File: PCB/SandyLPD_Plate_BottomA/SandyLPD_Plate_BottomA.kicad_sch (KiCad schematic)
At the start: 14 parts

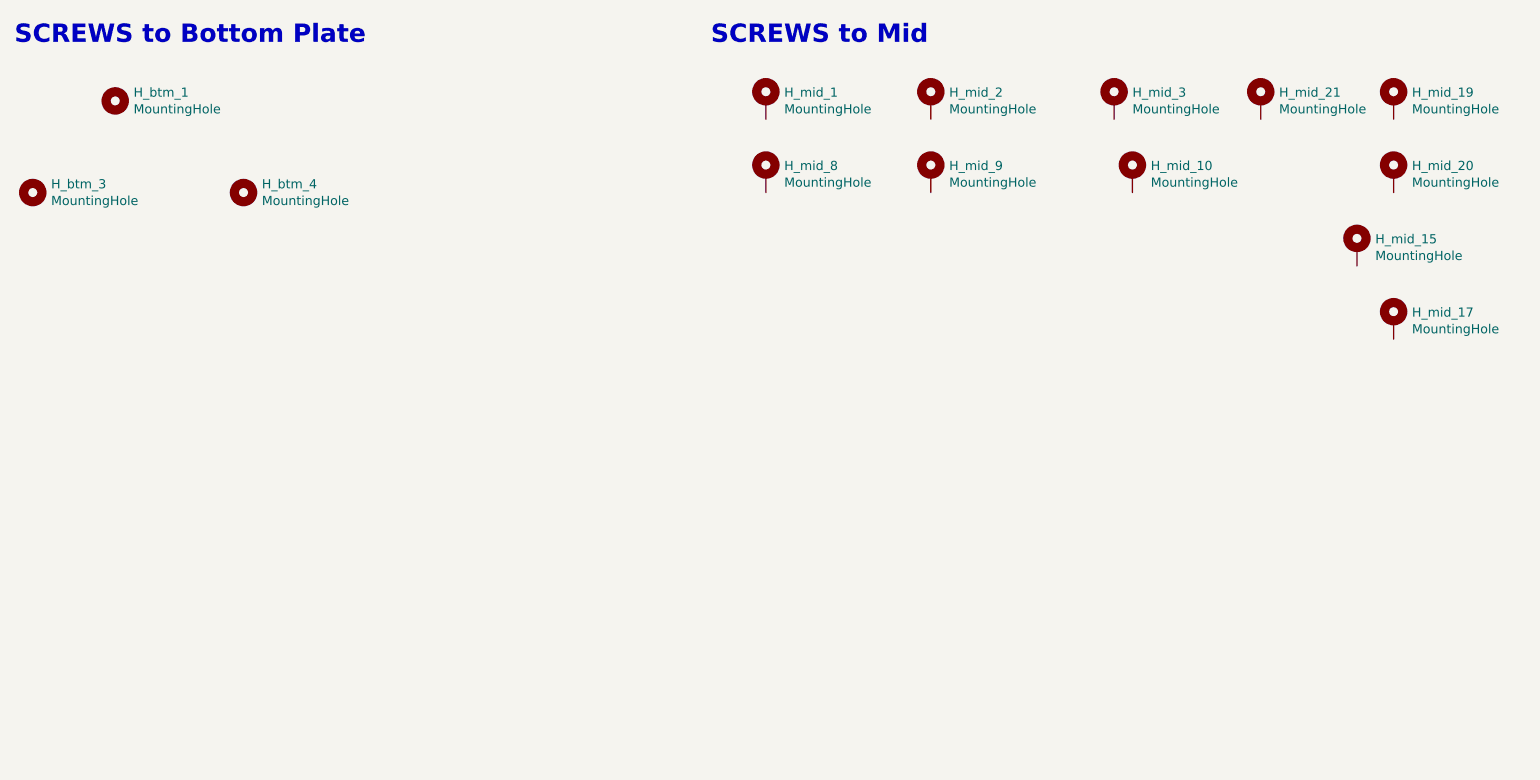
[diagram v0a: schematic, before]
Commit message: ソケット逃し穴の形状を変更
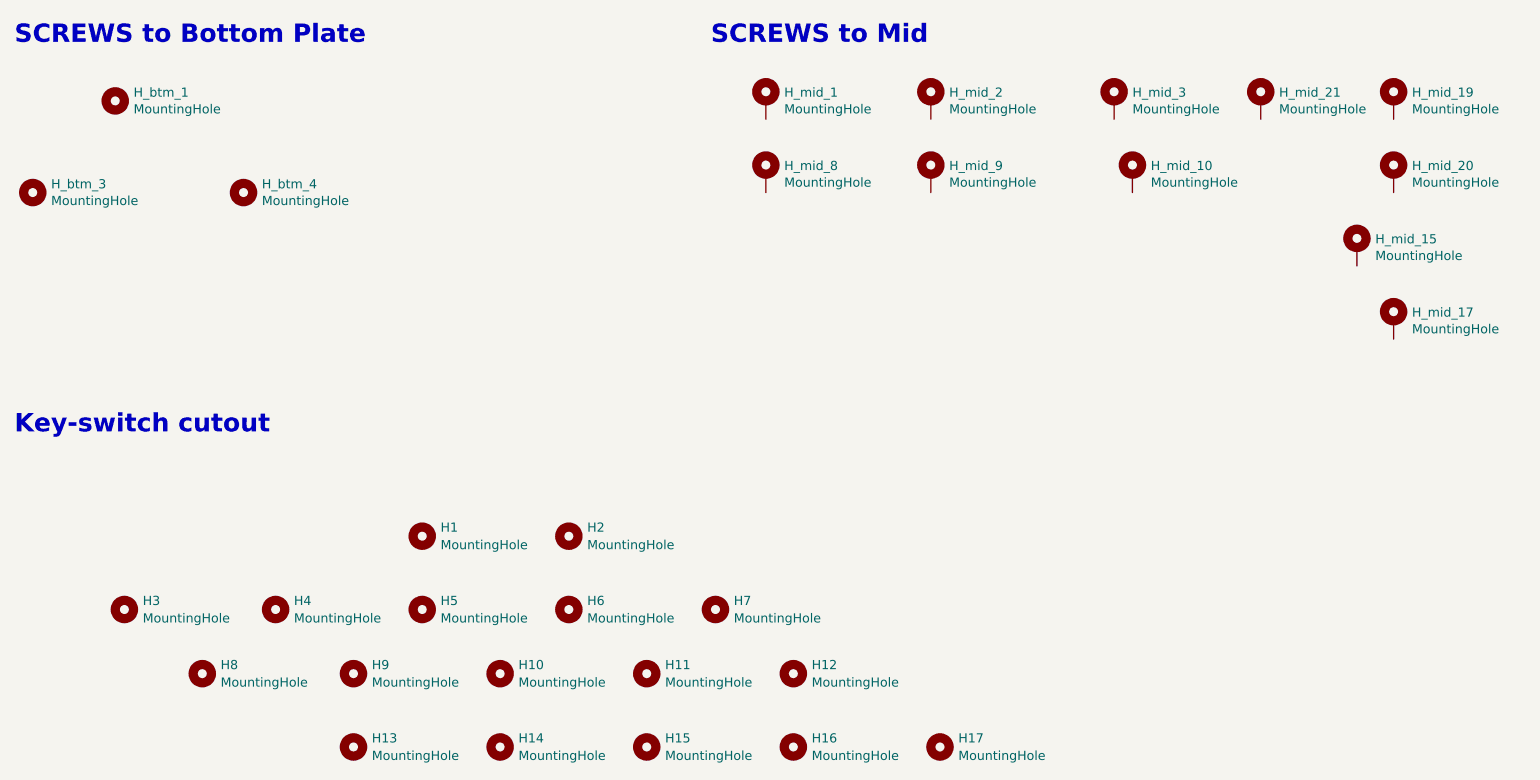
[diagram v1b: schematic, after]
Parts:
- added H1, H10, H11, H12, H14, H15, H16, H17, H2, H3, H4, H5, H6, H7, H8, H9: MountingHole, locallib:Kailh_socket_ChocV2_cutout_type2, symbol Mechanical:MountingHole
- added H13: MountingHole, locallib:Kailh_socket_ChocV2_and_RotaryEncoder_cutout_type2, symbol Mechanical:MountingHole
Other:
- note added: "Key-switch cutout"

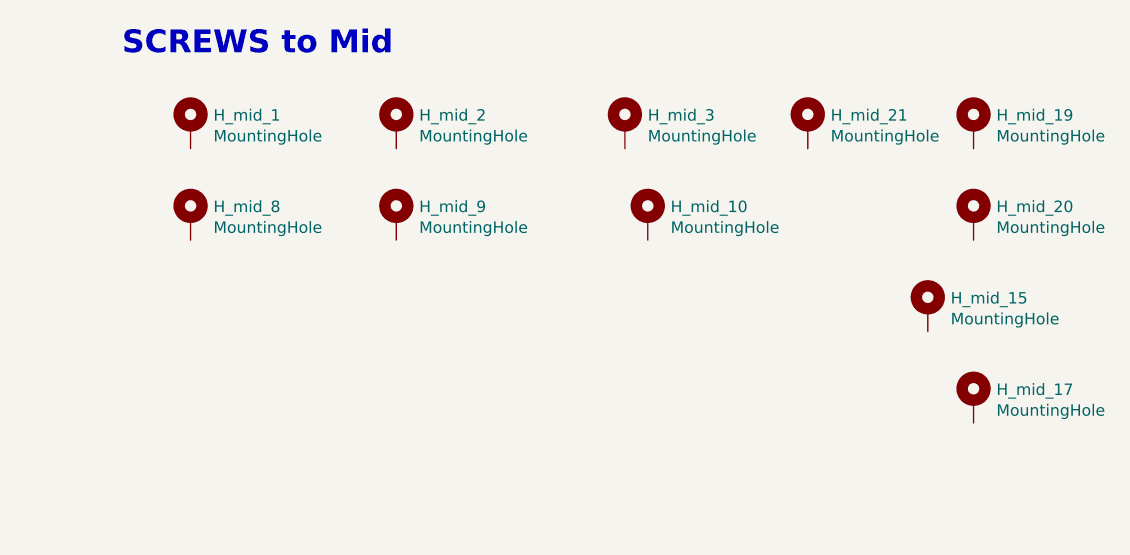
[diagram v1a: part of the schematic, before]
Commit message: EC11Kサポート廃止（新規設計非推奨のため）
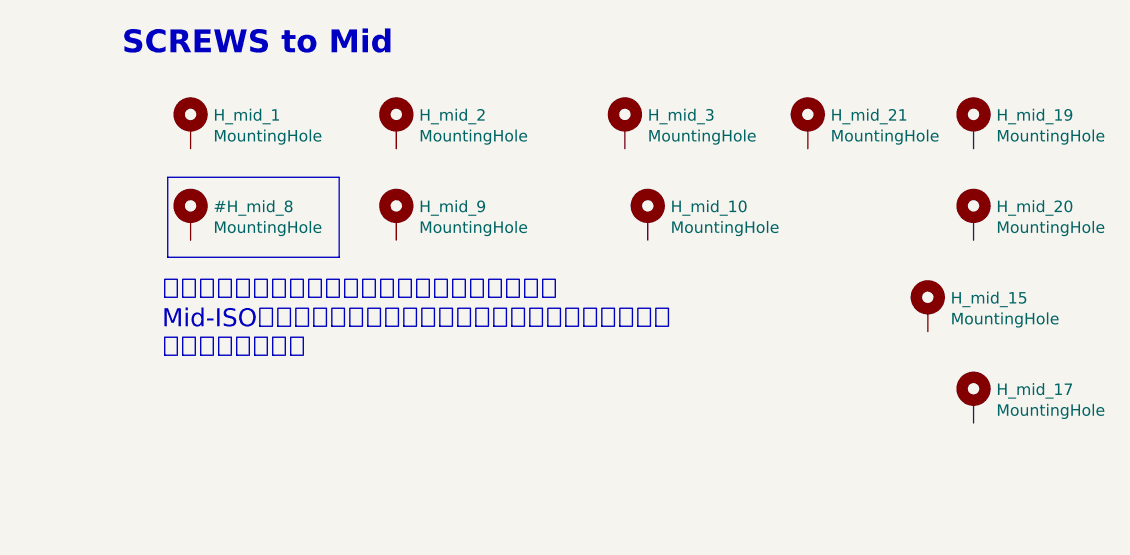
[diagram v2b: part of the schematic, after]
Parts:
- removed H_mid_8: MountingHole, locallib:MountingHole_2.2mm_M2_no_REF, symbol Mechanical:MountingHole_Pad
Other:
- note added: "ボトムプレートのサイズを少し小さくしたので、 Mid-ISO用ネジのひとつは、基板外形から出てしまうため、 穴を配置しない。"
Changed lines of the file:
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@@
 		(members "row0" "row5" "col0" "col1")
+	)
+	(rectangle
+		(start 130.81 60.96)
+		(end 149.86 69.85)
+		(stroke
+			(width 0)
+			(type default)
+		)
+		(fill
+			(type none)
+		)
 	)
 	(text "SCREWS to Mid"
@@
 		)
 	)
+	(text "ボトムプレートのサイズを少し小さくしたので、\nMid-ISO用ネジのひとつは、基板外形から出てしまうため、\n穴を配置しない。"
+		(exclude_from_sim no)
+		(at 130.175 76.835 0)
+		(effects
+			(font
+				(size 2 2)
+			)
+			(justify left)
+		)
+	)
 	(symbol
 		(lib_name "MountingHole_1")
@@
 		(on_board yes)
 		(dnp no)
-		(property "Reference" "H_mid_8"
+		(property "Reference" "#H_mid_8"
 			(at 135.89 64.2366 0)
 			(effects
@@
 			(project "SandyLP_Base"
 				(path "/a99ab643-cdc7-4f8c-8088-c1f4faa914d1"
-					(reference "H_mid_8")
-					(unit 1)
-				)
+					(reference "#H_mid_8")
+					(unit 1)
+				)

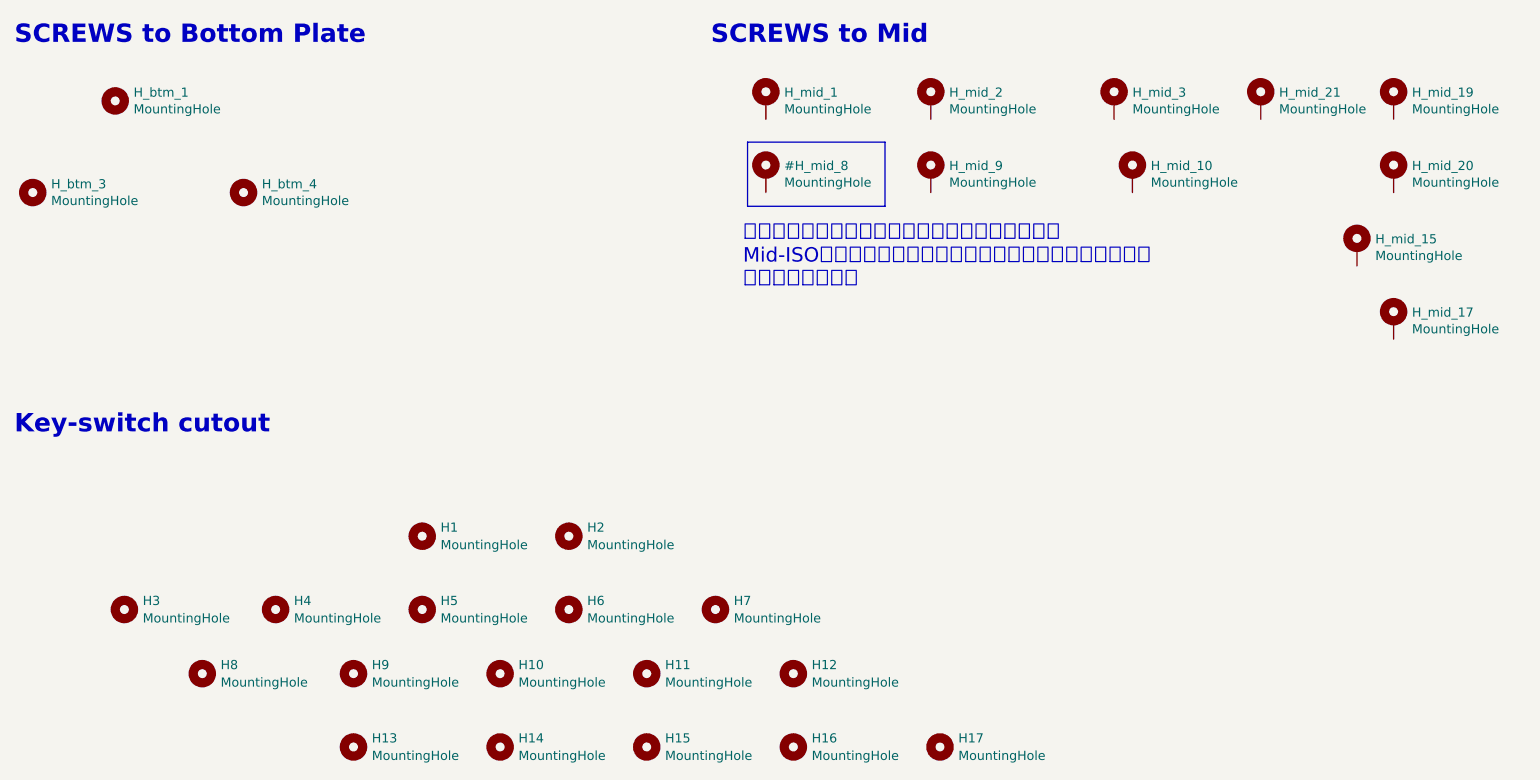
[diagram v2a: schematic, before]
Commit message: ボトムプレートの穴を大きく
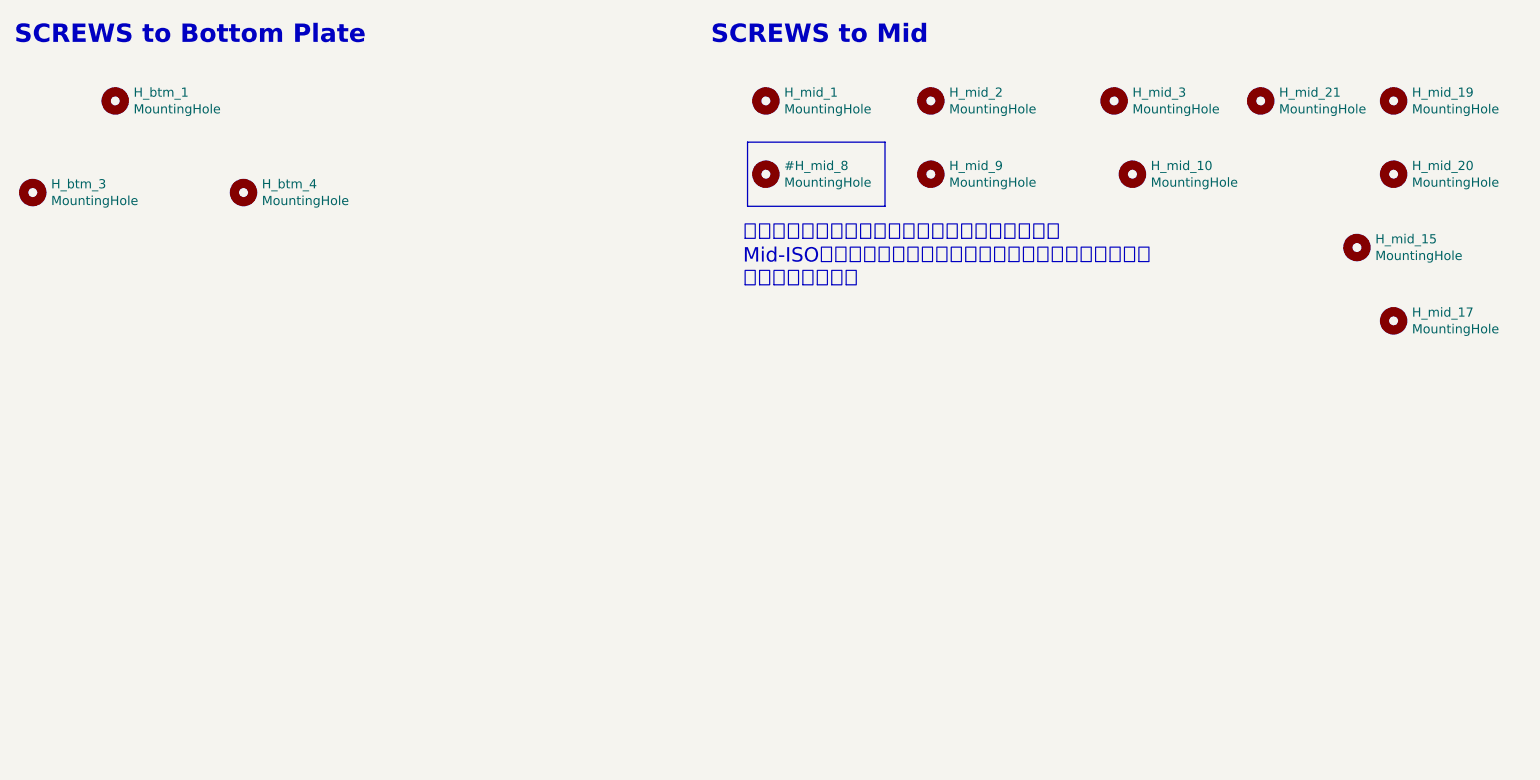
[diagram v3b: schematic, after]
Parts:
- removed H1, H10, H11, H12, H14, H15, H16, H17, H2, H3, H4, H5, H6, H7, H8, H9: MountingHole, locallib:Kailh_socket_ChocV2_cutout_type2, symbol Mechanical:MountingHole
- removed H13: MountingHole, locallib:Kailh_socket_ChocV2_and_RotaryEncoder_cutout_type2, symbol Mechanical:MountingHole
- H_mid_1, H_mid_10, H_mid_15, H_mid_17, H_mid_19, H_mid_2, H_mid_20, H_mid_21, H_mid_3, H_mid_9: symbol Mechanical:MountingHole_Pad -> Mechanical:MountingHole; now left out of the parts list
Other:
- note removed: "Key-switch cutout"

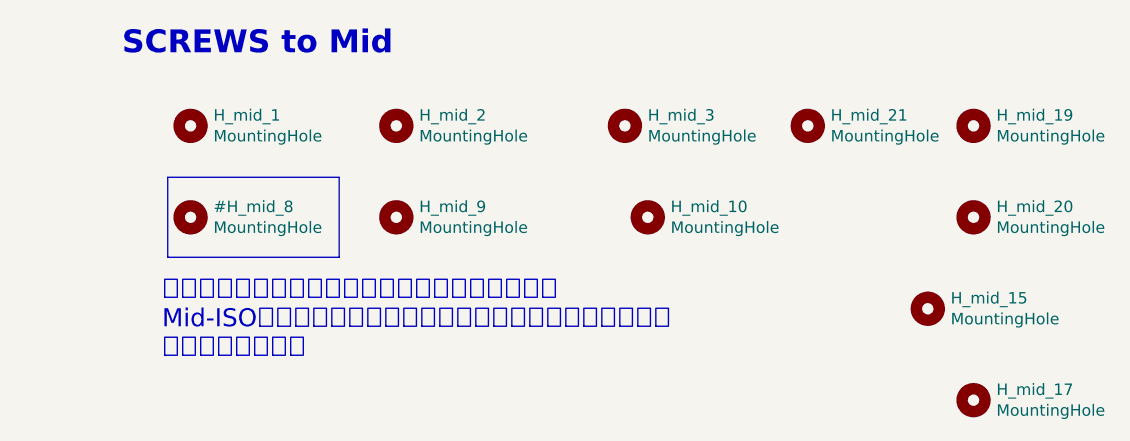
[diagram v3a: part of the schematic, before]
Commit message: ネジ穴位置を再調整。
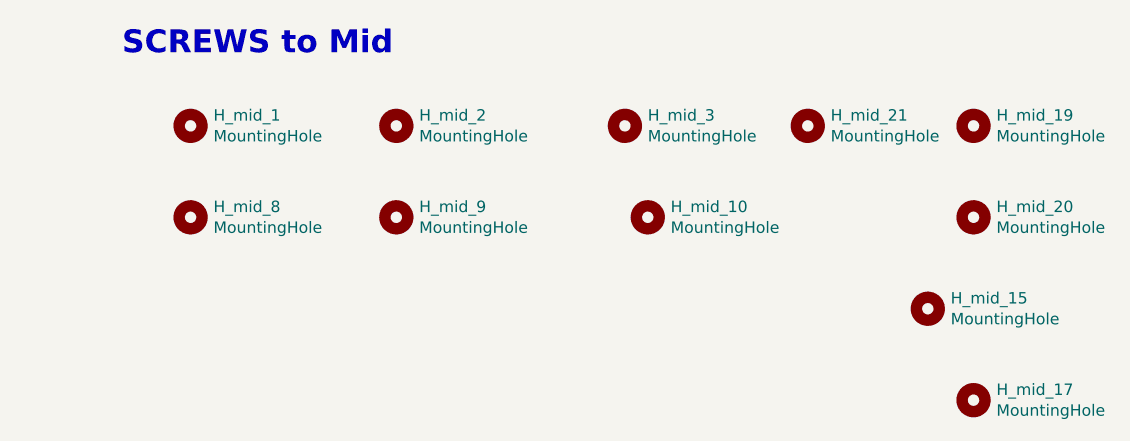
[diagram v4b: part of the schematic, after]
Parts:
- added H_mid_8: MountingHole, locallib:MountingHole_2.2mm_M2_no_REF, symbol Mechanical:MountingHole
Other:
- note removed: "ボトムプレートのサイズを少し小さくしたので、 Mid-ISO用ネジのひとつは、基板外形から出てしまうため、 穴を配置しない。"
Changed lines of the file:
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@@
 		(members "row0" "row5" "col0" "col1")
-	)
-	(rectangle
-		(start 130.81 60.96)
-		(end 149.86 69.85)
-		(stroke
-			(width 0)
-			(type default)
-		)
-		(fill
-			(type none)
-		)
 	)
 	(text "SCREWS to Mid"
@@
 			)
 			(justify left bottom)
-		)
-	)
-	(text "ボトムプレートのサイズを少し小さくしたので、\nMid-ISO用ネジのひとつは、基板外形から出てしまうため、\n穴を配置しない。"
-		(exclude_from_sim no)
-		(at 130.175 76.835 0)
-		(effects
-			(font
-				(size 2 2)
-			)
-			(justify left)
 		)
 	)
@@
 		(on_board yes)
 		(dnp no)
-		(property "Reference" "#H_mid_8"
+		(property "Reference" "H_mid_8"
 			(at 135.89 64.2366 0)
 			(effects
@@
 			(project "SandyLP_Base"
 				(path "/a99ab643-cdc7-4f8c-8088-c1f4faa914d1"
-					(reference "#H_mid_8")
+					(reference "H_mid_8")
 					(unit 1)
 				)
